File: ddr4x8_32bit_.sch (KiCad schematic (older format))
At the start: 4 parts

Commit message: Schematic capture update.
Schematic capture update.
DDR4 RAM page updated.
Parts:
- removed U? (x3): h5anag8ncmr-vkc, symbol hynix:h5anag8ncmr-vkc
- added C? (x36): 0.1uF, symbol Device:C_Small
- added C? (x8): 1uF, symbol Device:C_Small
- added R? (x4): 0R, symbol Device:R
- added R? (x4): DNP, symbol Device:R
- added R? (x4): 240R, symbol Device:R
- added U? (x3): h5anag8ncmr-vkc, symbol hynix:h5anag8ncmr-vkc
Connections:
- net labels added: DDR_VREF, VDD_DDR_VPP
- wire segments 104 -> 660
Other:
- note added: "DDR4 RAM"
- moved on the sheet: U?

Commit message: Schematic capture update.
Schematic capture update.  DDR4 section updated.
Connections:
- net labels added: DDR_A0, DDR_A1, DDR_A10, DDR_A11, DDR_A12, DDR_A13, DDR_A2, DDR_A3, DDR_A4, DDR_A5, DDR_A6, DDR_A7, DDR_A8, DDR_A9, DDR_ACT_N, DDR_A[13..0], DDR_CAS_N, DDR_DM0, DDR_DM1, DDR_DM2, DDR_DM3, DDR_DQ0, DDR_DQ1, DDR_DQ10, DDR_DQ11, DDR_DQ12, DDR_DQ13, DDR_DQ14, DDR_DQ15, DDR_DQ16, DDR_DQ17, DDR_DQ18, DDR_DQ19, DDR_DQ2, DDR_DQ20, DDR_DQ21, DDR_DQ22, DDR_DQ23, DDR_DQ3, DDR_DQ4, DDR_DQ5, DDR_DQ6, DDR_DQ7, DDR_DQ8, DDR_DQ9, DDR_DQS0_N, DDR_DQS0_P, DDR_DQS1_N, DDR_DQS1_P, DDR_DQS2_N, DDR_DQS2_P, DDR_DQS3_N, DDR_DQS3_P, DDR_DQSA_N, DDR_DQ[15..8], DDR_DQ[23..16], DDR_DQ[31..24], DDR_DQ[7..0], DDR_RAS_N, DDR_WE_N, DDR__DQ24, DDR__DQ25, DDR__DQ26, DDR__DQ27, DDR__DQ28, DDR__DQ29, DDR__DQ30, DDR__DQ31, DDR__DQS3_N, DDR__DQS3_P
- wire segments 660 -> 668

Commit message: Schematic capture update.
Schematic capture update.  DDR4 page updated.
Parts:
- added R? (x3): 33R, symbol Device:R
- added RN? (x7): R_Network04, Resistor_THT:R_Array_SIP5, symbol Device:R_Network04
- added U?: TPS51200DRC, Package_SON:VSON-10-1EP_3x3mm_P0.5mm_EP1.65x2.4mm, symbol Regulator_Linear:TPS51200DRC
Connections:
- net labels added: DDR_ALERT_N, DDR_BA0, DDR_BA1, DDR_BG0, DDR_BG1, DDR_CKE, DDR_CKE1, DDR_CLK_N, DDR_CLK_P, DDR_CS0_N, DDR_CS1_N, DDR_ODT, DDR_ODT1, DDR_PARITY_IN, DDR_RESET_N
- wire segments 668 -> 719
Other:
- moved on the sheet: C?, R?, U?

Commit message: Schematic capture update.
Schematic capture update(DDR).
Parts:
- added C? (x2): 10uF, symbol Device:C_Small
- added R? (x2): 0R001, symbol Device:R
- added R? (x2): 10K, symbol Device:R
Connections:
- net labels added: REFIN, VDD_3V3, VDD_DDR, VDD_DDRVPP_N, VDD_DDR_MEM_N, VDD_DDR_MEM_P, VDD_DRRVPP_P
- wire segments 719 -> 760
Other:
- note added: "TBD レイアウトノート"
- moved on the sheet: U?

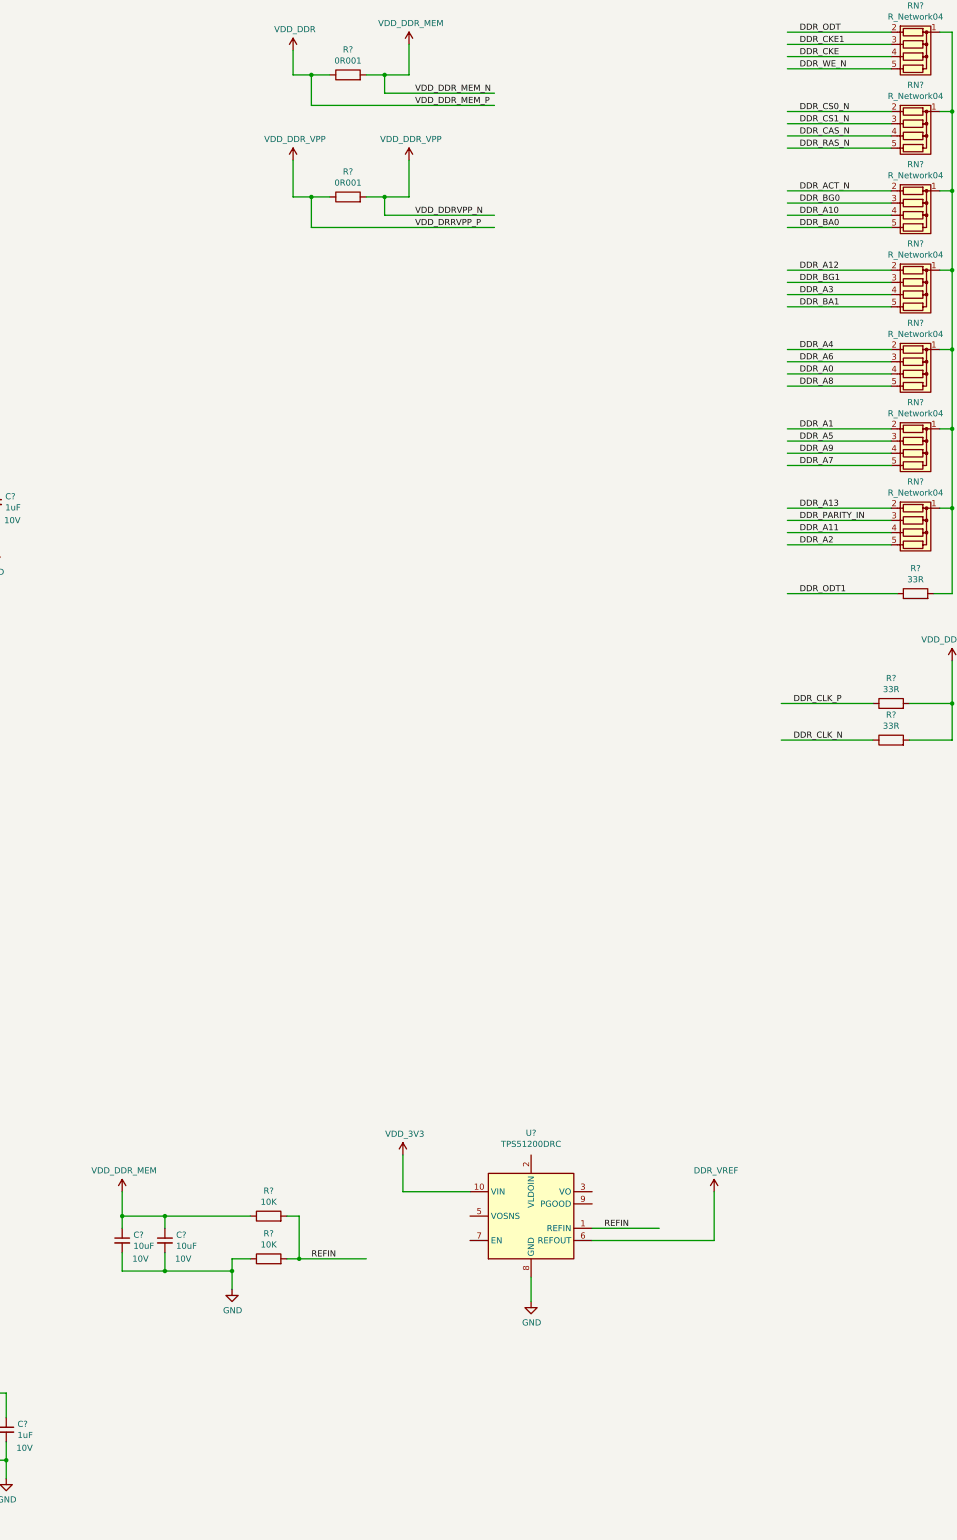
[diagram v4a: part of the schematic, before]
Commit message: Schematic capture update.
Schematic capture update(DDR4).
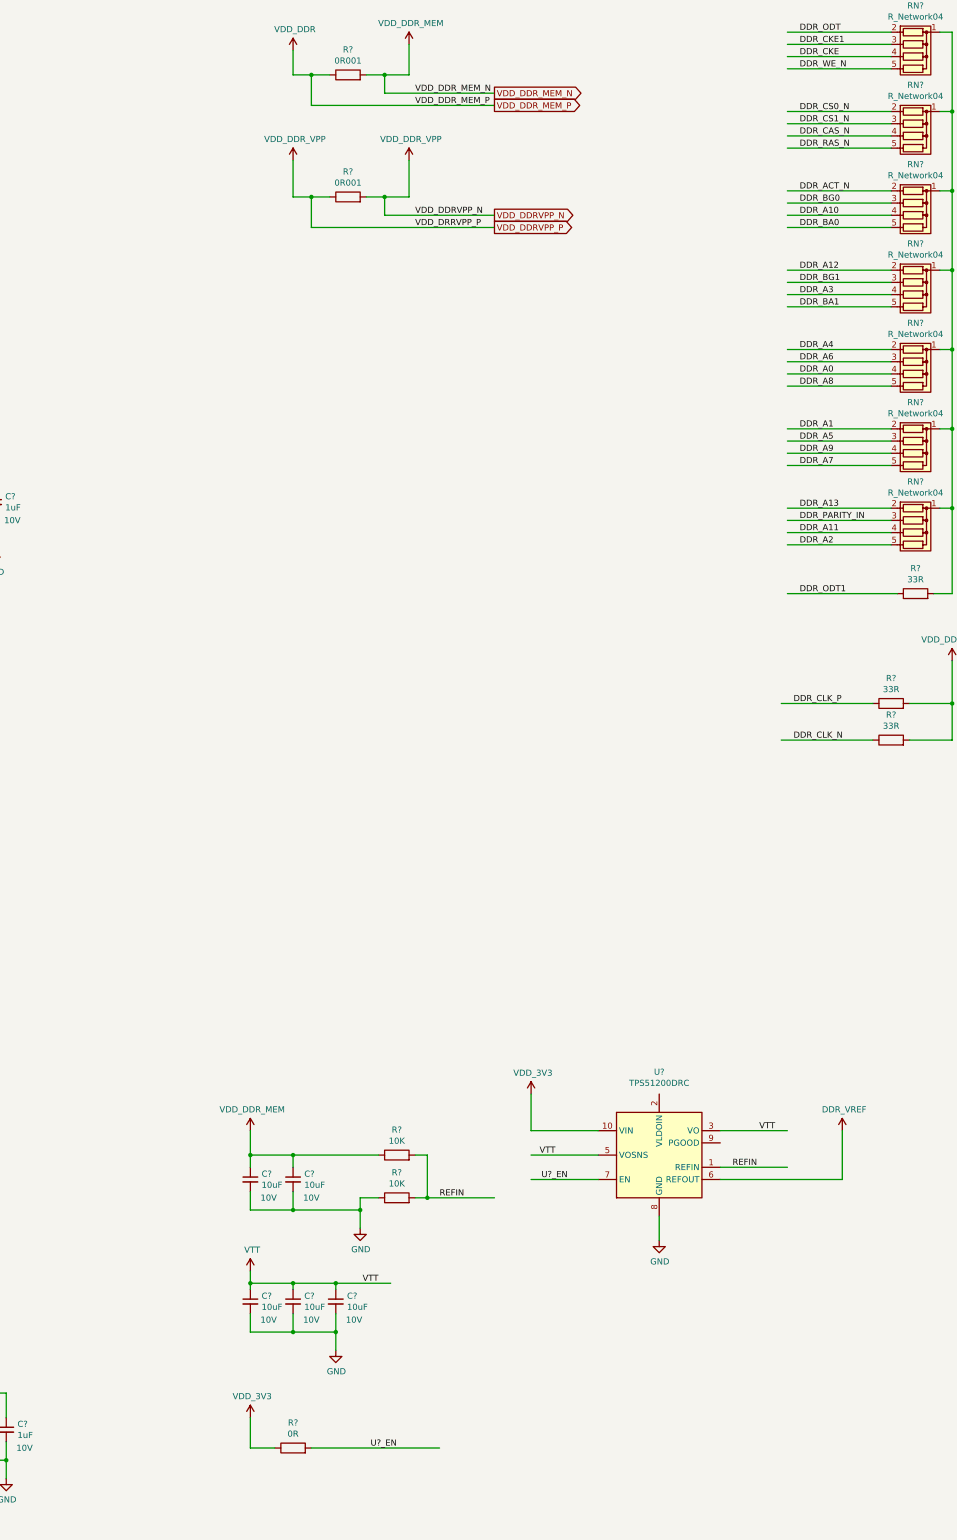
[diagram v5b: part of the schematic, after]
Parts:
- added C? (x3): 10uF, symbol Device:C_Small
- added R?: 0R, symbol Device:R
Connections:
- net labels added: U?_EN, VDD_DDRVPP_P, VTT
- wire segments 760 -> 779
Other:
- moved on the sheet: C?, R?, U?

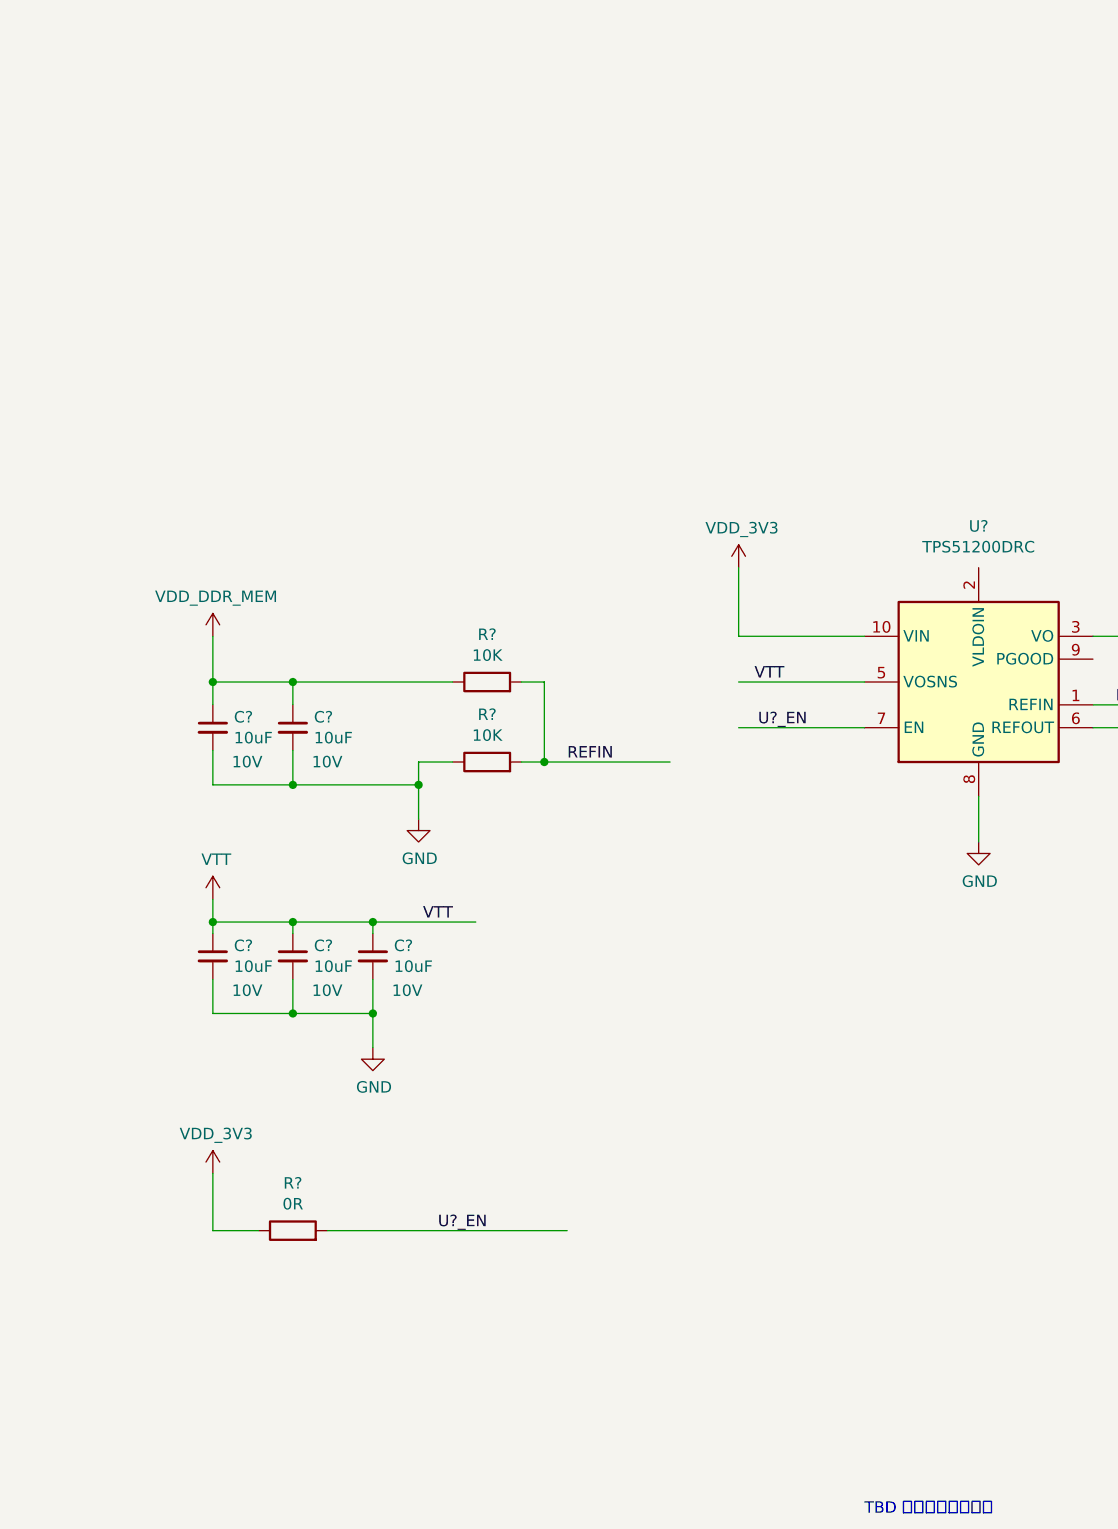
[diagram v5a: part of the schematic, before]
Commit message: Schematic capture update.
Schematic capture update (PCIe Page.)
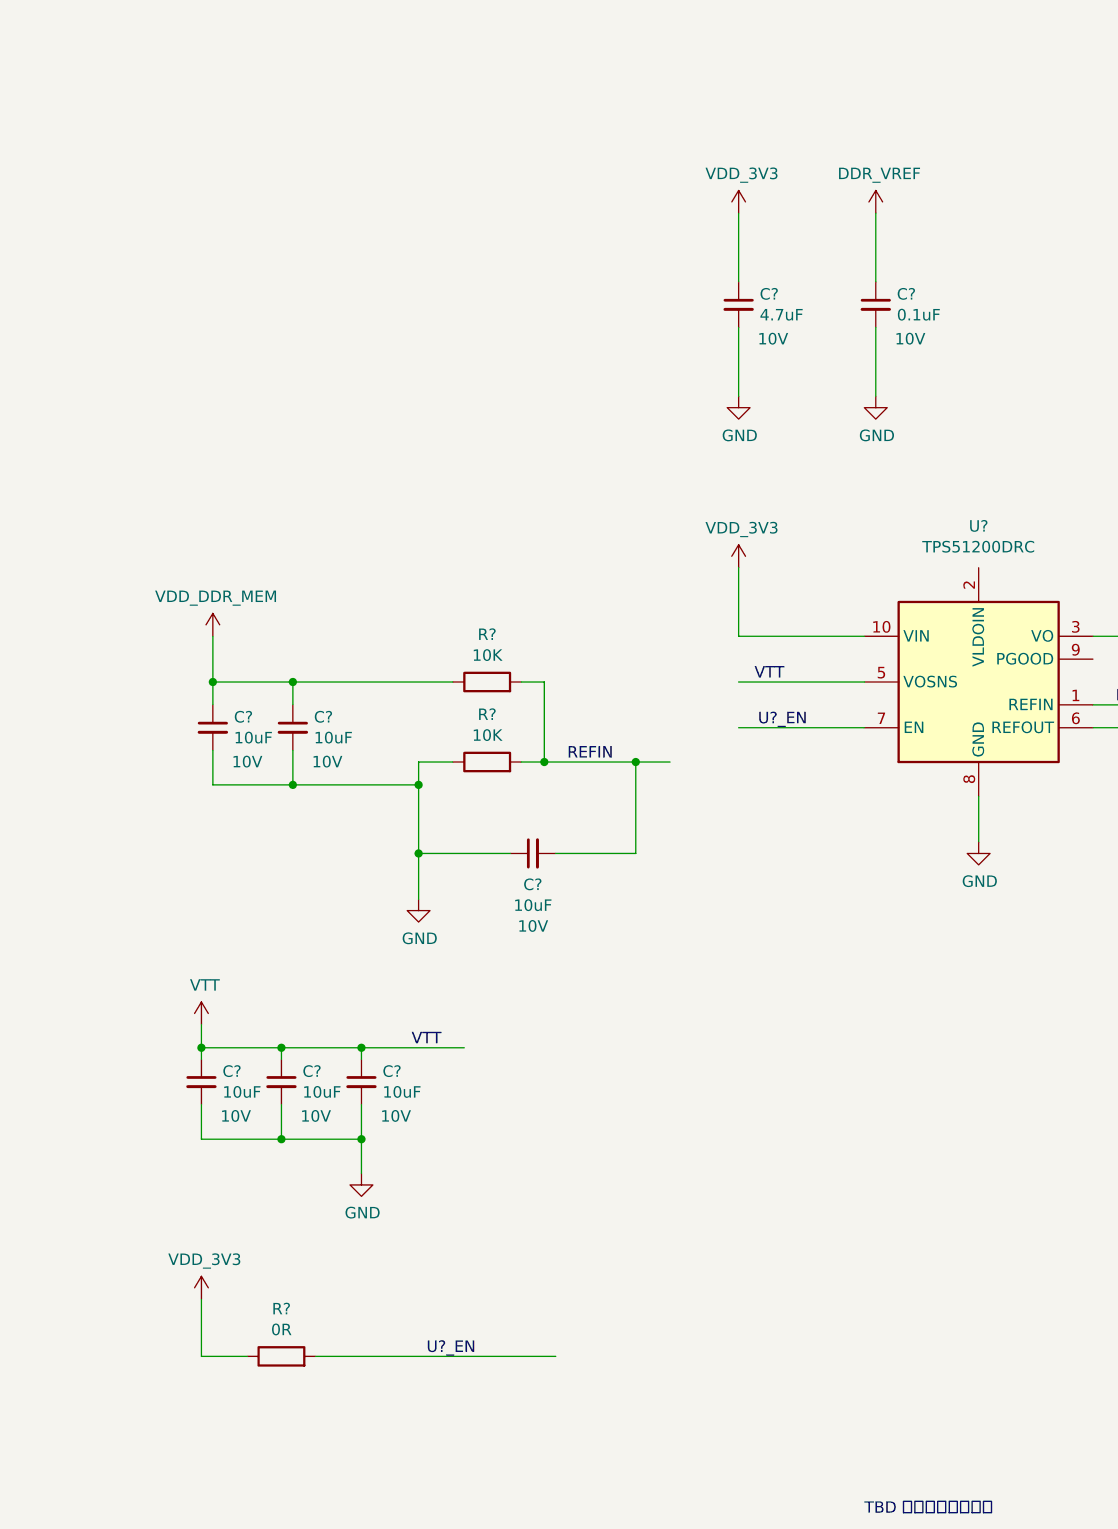
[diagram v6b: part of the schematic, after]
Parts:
- added C?: 4.7uF, symbol Device:C_Small
- added C?: 0.1uF, symbol Device:C_Small
- added C?: 10uF, symbol Device:C_Small
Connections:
- wire segments 779 -> 788
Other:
- moved on the sheet: C?, R?

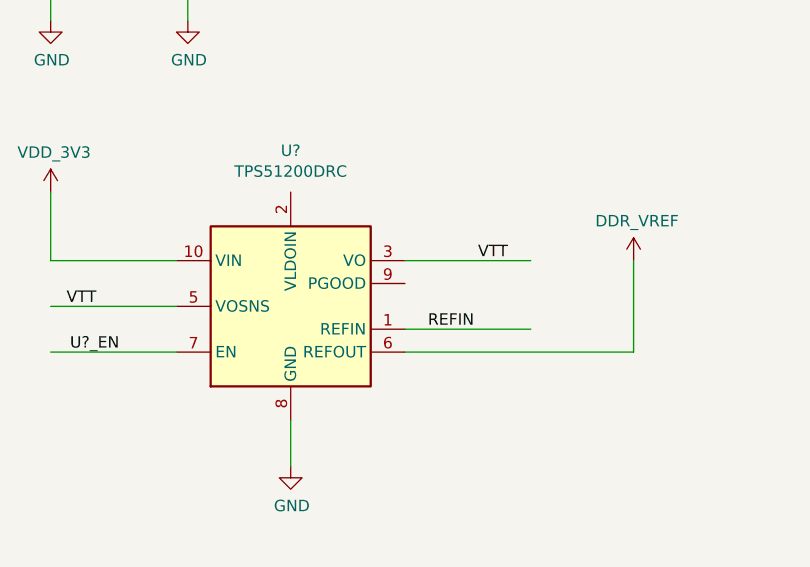
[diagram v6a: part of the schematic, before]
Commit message: Schematic capture update
Schematic capture update (PCIe)
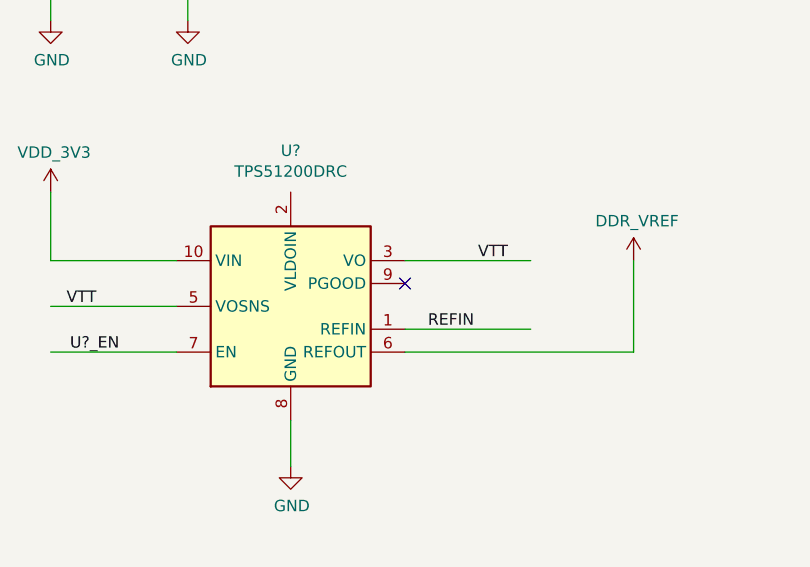
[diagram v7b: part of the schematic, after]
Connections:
- no-connect marks 0 -> 1
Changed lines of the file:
@@
 EndData
 $EndBitmap
+NoConn ~ 20450 10300
 Wire Bus Line
 	5850 10750 5850 11550
